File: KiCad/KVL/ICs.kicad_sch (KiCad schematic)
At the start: 47 parts, among them J1 AudioJack2_Ground, J2 Conn_01x04, J3 AudioJack2_Ground, J4 Conn_01x11, U1 74HC164, U2 74HC165, U3 74HC165, U5 ADAU1761BCPZ, U6 MIC2005A-1YM5-TR

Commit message: キースイッチをソケット化
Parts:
- RV1, RV2: footprint My_Parts:PTV09A4015UB103 -> My_Parts:RK09K1130A5R
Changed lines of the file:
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@@
       (effects (font (size 1.27 1.27)) (justify right))
     )
-    (property "Footprint" "My_Parts:PTV09A4015UB103" (at 38.1 67.31 0)
+    (property "Footprint" "My_Parts:RK09K1130A5R" (at 38.1 67.31 0)
       (effects (font (size 1.27 1.27)) hide)
     )
@@
       (effects (font (size 1.27 1.27)) (justify right))
     )
-    (property "Footprint" "My_Parts:PTV09A4015UB103" (at 38.1 45.72 0)
-      (effects (font (size 1.27 1.27)) hide)
-    )
+    (property "Footprint" "My_Parts:RK09K1130A5R" (at 38.1 45.72 0)
+      (effects (font (size 1.27 1.27)) hide)
+    )

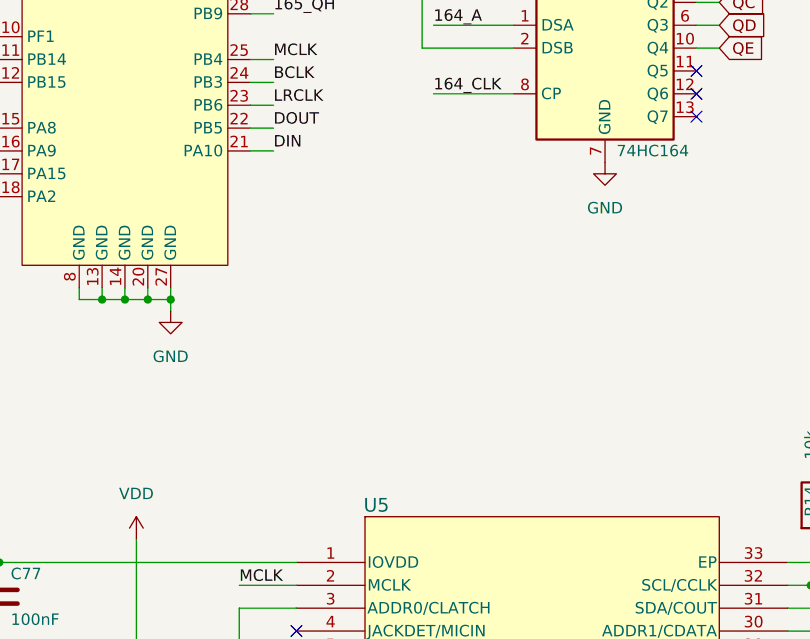
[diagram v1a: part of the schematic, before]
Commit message: Added Line/Phono Switching LED.
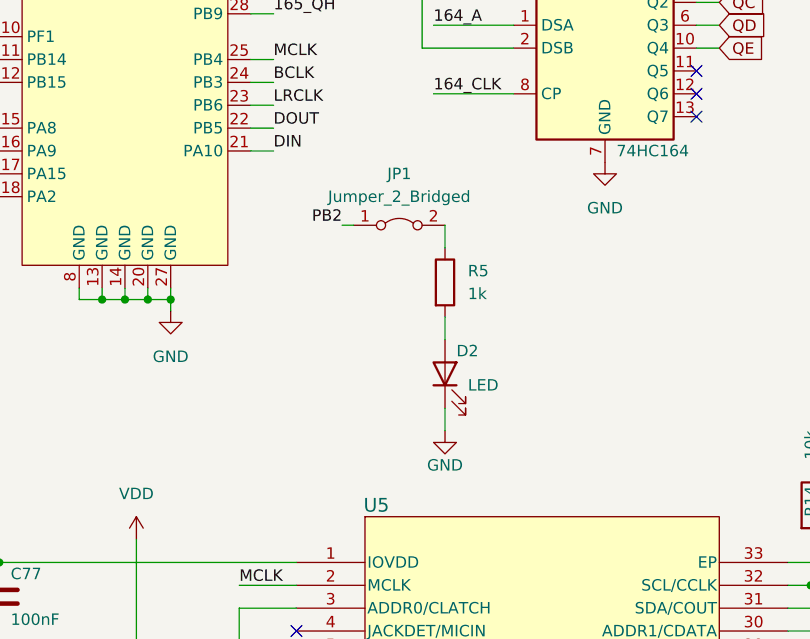
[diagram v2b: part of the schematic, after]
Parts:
- added D2: LED, LED_SMD:LED_0603_1608Metric, symbol Device:LED
- added JP1: Jumper_2_Bridged, Jumper:SolderJumper-2_P1.3mm_Bridged_RoundedPad1.0x1.5mm, symbol Jumper:Jumper_2_Bridged
- added R5: 1k, Resistor_SMD:R_0402_1005Metric, symbol Device:R
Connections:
- net GND: now also D2.1 (K)
- net PB2: now also JP1.1 (A)
- new net: D2.2 (A), R5.2
- new net: JP1.2 (B), R5.1
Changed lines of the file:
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@@
+    (stroke (width 0) (type default))
+  )
+  (wire (pts (xy 105.41 84.455) (xy 105.41 86.995))
     (stroke (width 0) (type default))
   )
@@
     (stroke (width 0) (type default))
   )
+  (wire (pts (xy 105.41 104.775) (xy 105.41 107.315))
+    (stroke (width 0) (type default))
+  )
   (wire (pts (xy 172.72 139.7) (xy 172.72 144.78))
     (stroke (width 0) (type default))
@@
     (stroke (width 0) (type default))
   )
+  (wire (pts (xy 93.98 84.455) (xy 95.25 84.455))
+    (stroke (width 0) (type default))
+  )
   (wire (pts (xy 205.74 128.27) (xy 205.74 130.81))
     (stroke (width 0) (type default))
@@
     (stroke (width 0) (type default))
   )
+  (wire (pts (xy 105.41 94.615) (xy 105.41 97.155))
+    (stroke (width 0) (type default))
+  )
   (label "PB15" (at 50.8 68.58 0) (fields_autoplaced)
     (effects (font (size 1.27 1.27)) (justify left bottom))
@@
   (label "PA15" (at 36.83 91.44 0) (fields_autoplaced)
     (effects (font (size 1.27 1.27)) (justify left bottom))
+  )
+  (label "PB2" (at 93.98 84.455 180) (fields_autoplaced)
+    (effects (font (size 1.27 1.27)) (justify right bottom))
   )
   (label "PA2" (at 36.83 93.98 0) (fields_autoplaced)
@@
         (path "/95d3b5cf-f65f-442c-bf39-1d0330504361/b501dded-0795-4b94-b467-4024a4d9920f"
           (reference "#PWR03") (unit 1)
+        )
+      )
+    )
+  )
+  (symbol (lib_id "Device:LED") (at 105.41 100.965 90) (unit 1)
+    (in_bom yes) (on_board yes) (dnp no)
+    (property "Reference" "D2" (at 106.68 98.425 90)
+      (effects (font (size 1.27 1.27)) (justify right))
+    )
+    (property "Value" "LED" (at 107.95 102.235 90)
+      (effects (font (size 1.27 1.27)) (justify right))
+    )
+    (property "Footprint" "LED_SMD:LED_0603_1608Metric" (at 105.41 100.965 0)
+      (effects (font (size 1.27 1.27)) hide)
+    )
+    (property "Datasheet" "~" (at 105.41 100.965 0)
+      (effects (font (size 1.27 1.27)) hide)
+    )
+    (pin "1")
+    (pin "2")
+    (instances
+      (project "C4NDY"
+        (path "/868f46d4-ce7a-4a96-bb33-8a76e5eb710a"
+          (reference "D2") (unit 1)
+        )
+      )
+      (project "KVL"
+        (path "/95d3b5cf-f65f-442c-bf39-1d0330504361/b501dded-0795-4b94-b467-4024a4d9920f"
+          (reference "D66") (unit 1)
+        )
+      )
+      (project "C4NDY_XMOS"
+        (path "/d1ba3648-626f-4274-af64-5bb23c676618"
+          (reference "D2") (unit 1)
         )
       )
@@
     )
   )
+  (symbol (lib_id "power:GND") (at 105.41 107.315 0) (unit 1)
+    (in_bom yes) (on_board yes) (dnp no)
+    (property "Reference" "#PWR031" (at 105.41 113.665 0)
+      (effects (font (size 1.27 1.27)) hide)
+    )
+    (property "Value" "GND" (at 105.41 111.125 0)
+      (effects (font (size 1.27 1.27)))
+    )
+    (property "Footprint" "" (at 105.41 107.315 0)
+      (effects (font (size 1.27 1.27)) hide)
+    )
+    (property "Datasheet" "" (at 105.41 107.315 0)
+      (effects (font (size 1.27 1.27)) hide)
+    )
+    (pin "1")
+    (instances
+      (project "C4NDY"
+        (path "/868f46d4-ce7a-4a96-bb33-8a76e5eb710a"
+          (reference "#PWR031") (unit 1)
+        )
+      )
+      (project "KVL"
+        (path "/95d3b5cf-f65f-442c-bf39-1d0330504361/b501dded-0795-4b94-b467-4024a4d9920f"
+          (reference "#PWR031") (unit 1)
+        )
+      )
+      (project "C4NDY_XMOS"
+        (path "/d1ba3648-626f-4274-af64-5bb23c676618"
+          (reference "#PWR037") (unit 1)
+        )
+      )
+    )
+  )
   (symbol (lib_id "power:GND") (at 190.5 41.91 0) (unit 1)
     (in_bom yes) (on_board yes) (dnp no) (fields_autoplaced)
@@
     )
   )
+  (symbol (lib_id "Jumper:Jumper_2_Bridged") (at 100.33 84.455 0) (unit 1)
+    (in_bom yes) (on_board yes) (dnp no) (fields_autoplaced)
+    (property "Reference" "JP1" (at 100.33 78.74 0)
+      (effects (font (size 1.27 1.27)))
+    )
+    (property "Value" "Jumper_2_Bridged" (at 100.33 81.28 0)
+      (effects (font (size 1.27 1.27)))
+    )
+    (property "Footprint" "Jumper:SolderJumper-2_P1.3mm_Bridged_RoundedPad1.0x1.5mm" (at 100.33 84.455 0)
+      (effects (font (size 1.27 1.27)) hide)
+    )
+    (property "Datasheet" "~" (at 100.33 84.455 0)
+      (effects (font (size 1.27 1.27)) hide)
+    )
+    (pin "2")
+    (pin "1")
+    (instances
+      (project "KVL"
+        (path "/95d3b5cf-f65f-442c-bf39-1d0330504361/b501dded-0795-4b94-b467-4024a4d9920f"
+          (reference "JP1") (unit 1)
+        )
+      )
+    )
+  )
   (symbol (lib_id "power:GND") (at 45.72 190.5 0) (unit 1)
     (in_bom yes) (on_board yes) (dnp no) (fields_autoplaced)
@@
           (reference "R7") (unit 1)
         )
+      )
+    )
+  )
+  (symbol (lib_id "Device:R") (at 105.41 90.805 0) (unit 1)
+    (in_bom yes) (on_board yes) (dnp no) (fields_autoplaced)
+    (property "Reference" "R5" (at 107.95 89.535 0)
+      (effects (font (size 1.27 1.27)) (justify left))
+    )
+    (property "Value" "1k" (at 107.95 92.075 0)
+      (effects (font (size 1.27 1.27)) (justify left))
+    )
+    (property "Footprint" "Resistor_SMD:R_0402_1005Metric" (at 103.632 90.805 90)
+      (effects (font (size 1.27 1.27)) hide)
+    )
+    (property "Datasheet" "~" (at 105.41 90.805 0)
+      (effects (font (size 1.27 1.27)) hide)
+    )
+    (pin "1")
+    (pin "2")
+    (instances
+      (project "C4NDY"
+        (path "/868f46d4-ce7a-4a96-bb33-8a76e5eb710a"
+          (reference "R5") (unit 1)
+        )
+      )
+      (project "KVL"
+        (path "/95d3b5cf-f65f-442c-bf39-1d0330504361/b501dded-0795-4b94-b467-4024a4d9920f"
+          (reference "R21") (unit 1)
+        )
+      )
+      (project "C4NDY_XMOS"
+        (path "/d1ba3648-626f-4274-af64-5bb23c676618"
+          (reference "R7") (unit 1)
+        )
